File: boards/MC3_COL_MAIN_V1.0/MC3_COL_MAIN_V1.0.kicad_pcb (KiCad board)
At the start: 4 copper layers, 66 x 66 mm, 101 parts, among them J1 SUPPLY_IN, J10 MOTOR, J11 MOTOR, J12 CAN, J2 SWD, J3 ENC_leaf1, J4 ENC_leaf2, J5 ENC_leaf3, J6 ENC_leaf4, J7 MOTOR, J8 MOTOR, J9 MOTOR, Q1 AO4407C, SW1 SKRKAEE020, U1 AMS1117-3.3, U2 STM32F412RET6, U3 DRV8214RTER, U4 DRV8214RTER, U5 DRV8214RTER, U6 DRV8214RTER, U7 DRV8214RTER, U8 TJA1051T/3, Y1 8MHz

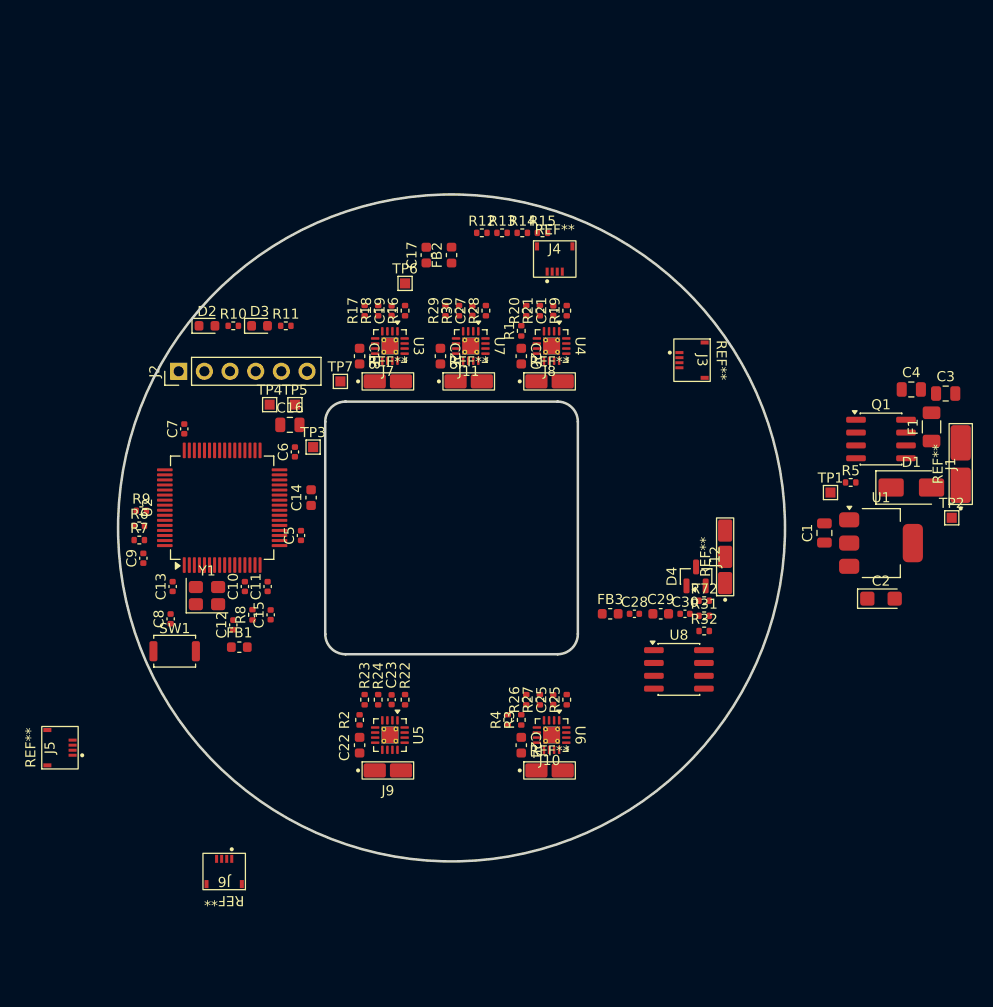
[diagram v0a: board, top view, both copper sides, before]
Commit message: PCB: user-facing items flipped to B.Cu; leaf3 pattern of record
Flipped 13 footprints to the back so they stay reachable once the board is
mounted component-face-toward-the-mechanism: J2 SWD, SW1 reset, D2/D3 LEDs,
J1 supply pads, J12 CAN pads, TP1-TP7. 88 footprints remain on F.Cu.

Of those, only SW1, D2 and D3 have any assembly cost - the pads are bare copper
and J2 is through-hole, so the SMT process stays single-sided unless those three
stay on the back. Noted so the choice can be reversed cheaply.

DRC after the flip: 275 unconnected (nothing routed yet), no new errors;
warnings 296 -> 229 as the user's hand-deleted REF** texts came out.

Board also carries the user's leaf3 rework: the whole block rotated one 90 deg
step and moved outboard, driver at r=25.2 and motor pads at r=26.6, pads facing
the rim. MIGRATION records the turned pattern as the block of record and marks
the placement of leaf1/leaf2/leaf4/yaw as the user's, per their decision.

flip_component has no IPC path - it writes the file directly and refuses while
KiCad is running, so further flips are a quit-KiCad operation.

Co-Authored-By: Claude Opus 5 (1M context) <noreply@anthropic.com>
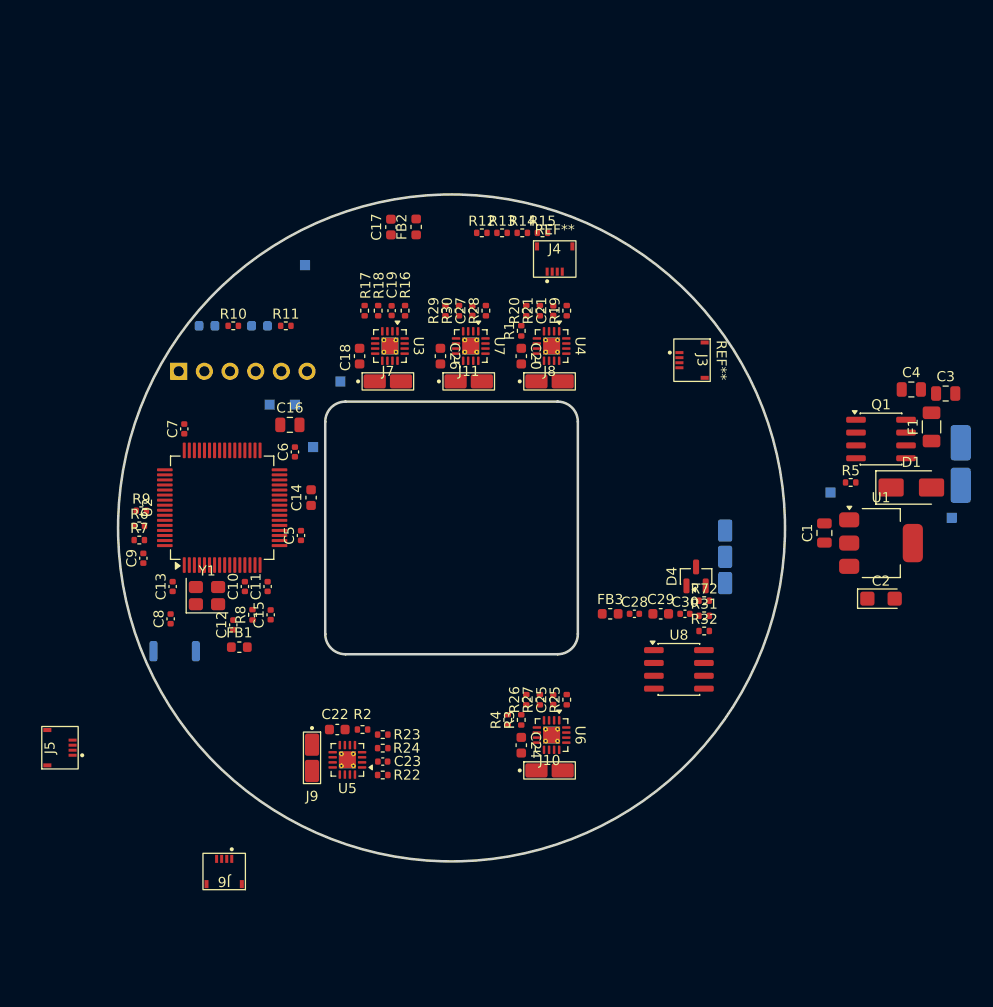
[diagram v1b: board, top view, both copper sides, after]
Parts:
- D2, D3, J1, J12, J2, SW1, TP1, TP2, TP3, TP4, TP5, TP6, TP7: moved to B.Cu
- moved TP6 10.1 mm to (85.5, 74.0)
- moved R22 7.77 mm to (93.2, 124.5), turned to 0 degrees
- moved J9 7.61 mm to (86.2, 122.8), turned to -90 degrees
- moved C23 6.18 mm to (93.2, 123.1), turned to 0 degrees
- moved U5 4.87 mm to (89.7, 123.0), turned to 180 degrees
- moved R24 4.81 mm to (93.2, 121.8), turned to 0 degrees
- moved FB2 4.47 mm to (96.5, 70.2)
- moved C17 4.47 mm to (94.0, 70.2)
- moved R23 3.89 mm to (93.2, 120.5), turned to 0 degrees
- moved C22 2.70 mm to (88.7, 120.0), turned to 180 degrees
- moved R2 0.99 mm to (91.2, 120.0), turned to 0 degrees
- turned J1 to -90 degrees
- turned J12 to -90 degrees
- turned J2 to -90 degrees

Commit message: PCB: add the three copper zones (In1 GND, In2 +3V3, B.Cu GND)
Written with KiCad quit - add_zone has no IPC path. Each zone is a rectangle
loosely enclosing the board (66,66)-(134,134); KiCad clips the fill to the
outline and to the central aperture, so no polygon has to trace the disc.
Clearance 0.2, min width 0.2, matching the MOTOR/VM netclass clearance.

Plane allocation changed from the earlier plan (In2 was to be VM). The pad
counts are lopsided - +3V3 has 55 pads spread across the whole disc while VM
has 20 clustered ones - so In2 carries +3V3 and VM becomes a 2.0 mm trunk on
F.Cu, where the high-current loop can be seen and shaped. The 2 A polyfuse
caps sustained VM current, so the trunk is thermally easy. A higher-priority
VM island can be dropped onto In2 under the motor annulus once the channels
are placed, which gets both.

In1 stays solid GND: it is the return reference 0.21 mm below every F.Cu
trace, which is what makes top-side routing good.

The zones carry no fill data yet - they need Edit > Fill All Zones (B) and a
save in KiCad before connectivity counts them. Expect unconnected to fall from
271 to roughly 120 at that point.

Co-Authored-By: Claude Opus 5 (1M context) <noreply@anthropic.com>
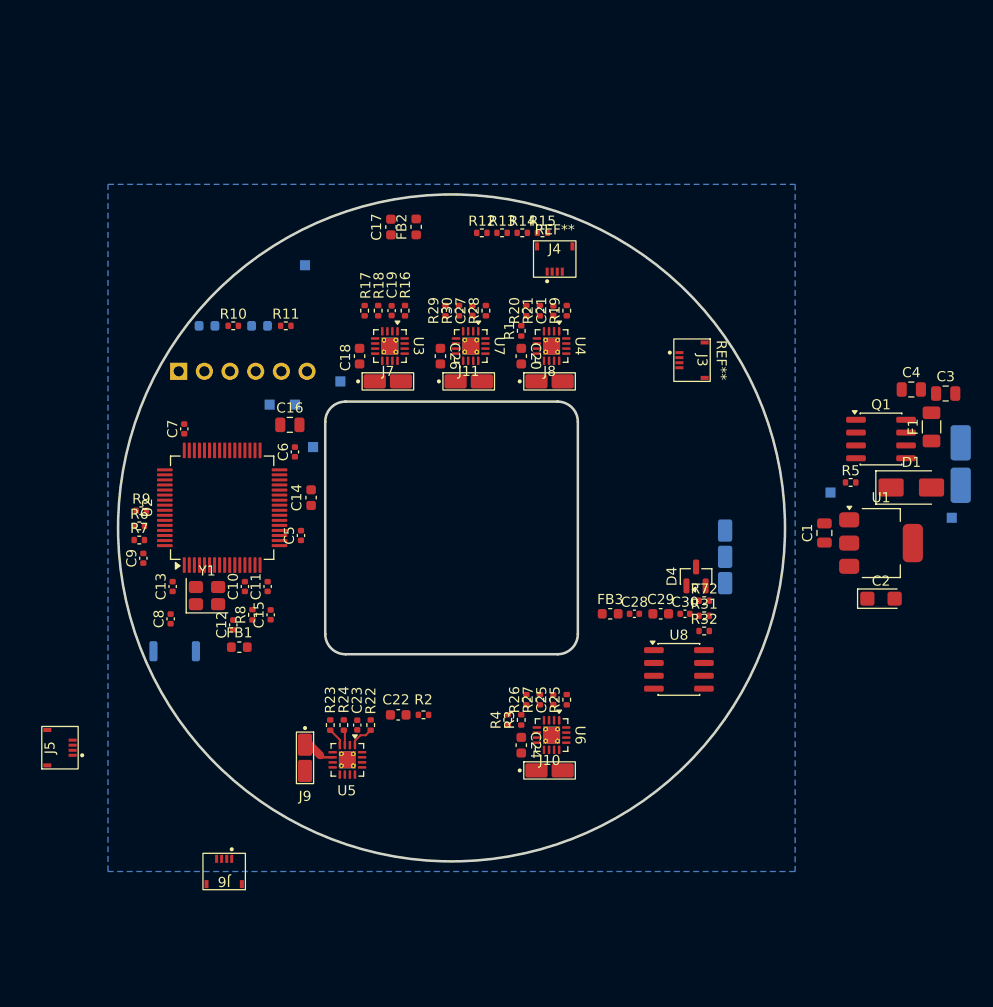
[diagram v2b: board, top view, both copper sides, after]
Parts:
- moved C22 6.21 mm to (94.7, 118.5)
- moved R2 6.21 mm to (97.2, 118.5)
- moved R23 5.28 mm to (88.0, 119.5), turned to -90 degrees
- moved R22 5.08 mm to (92.0, 119.5), turned to 90 degrees
- moved R24 4.48 mm to (89.3, 119.5), turned to -90 degrees
- moved C23 4.40 mm to (90.7, 119.5), turned to 90 degrees
- moved J9 0.69 mm to (85.5, 122.8)
- turned U5 to -90 degrees
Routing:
- net /leaf3/OUT1: track 0.00 -> 3.25 mm
- net IPROPI_leaf3: track 0.00 -> 2.42 mm
- net nFAULT_leaf3: track 0.00 -> 1.86 mm
- net RC_OUT_leaf3: track 0.00 -> 1.52 mm
- added copper zone on In2.Cu, net +3V3
- added copper zone on B.Cu, net GND
- added copper zone on In1.Cu, net GND

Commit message: PCB: F.Cu GND pour, 34 GND stitching vias, first leaf3 routing
User added the F.Cu GND zone and set In1 to solid pad connection; Konnect added
34 through-hole stitching vias (0.6/0.3) on a ~7 mm grid, positions computed
against all 415 pads and the existing traces so none creates a clearance error.
User also rotated U5 to -90 so the driver's power edge (pins 5-8) now faces the
motor pads, and routed the first leaf3 traces (21 segments).

Connectivity: 275 -> 204 unconnected. The whole gain came from the F.Cu pour;
the stitching vias moved nothing, because each DRV8214 exposed pad already
carries four through-holes that bridged F.Cu / In1 / B.Cu, so GND was already
one body. The vias are kept for return-path quality and to tie in pour islands
as routing fragments the top layer.

What is left, by net: +3V3 42 pads, VM 14, signals ~120, and GND just 7 - and
all 7 (C2.2, C4.2, D1.2, J1.2, R5.2, U1.1, J6.2) are parts still parked outside
the board outline, where no zone fills.

Co-Authored-By: Claude Opus 5 (1M context) <noreply@anthropic.com>
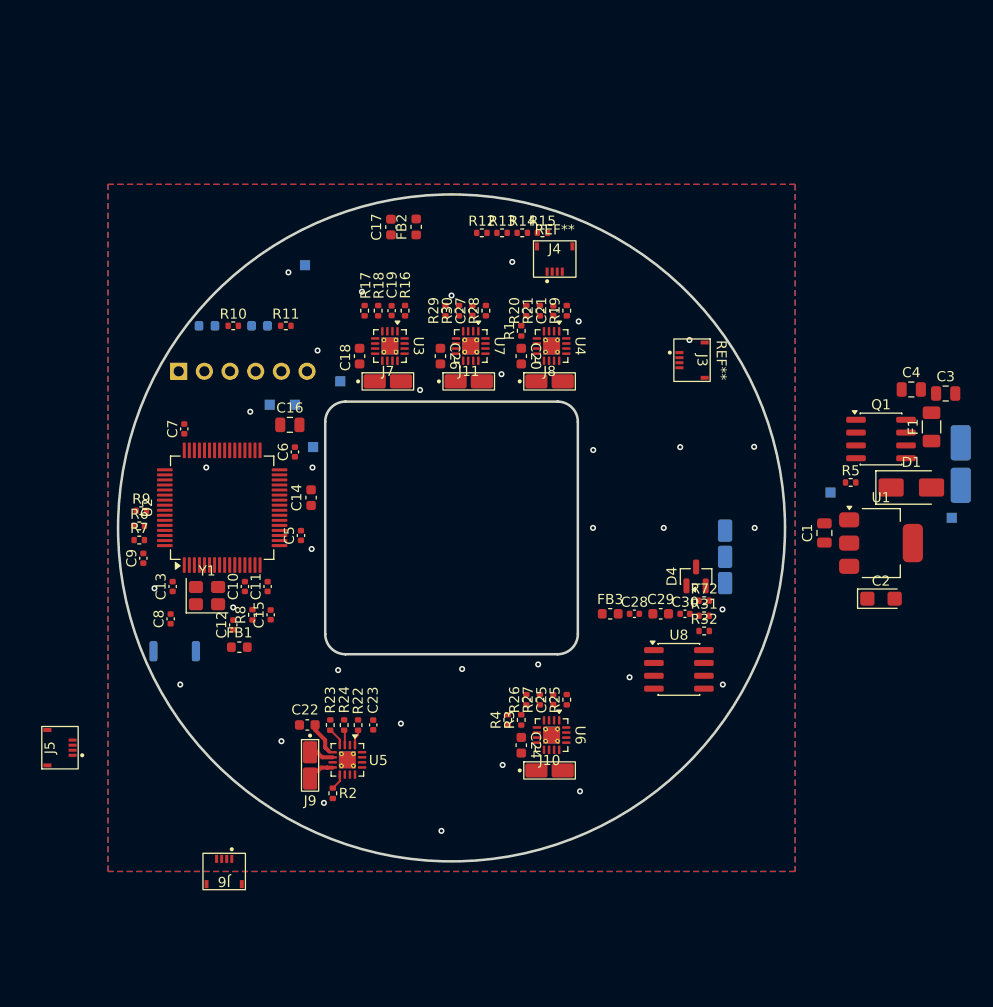
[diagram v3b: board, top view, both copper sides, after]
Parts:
- moved R2 11.9 mm to (88.2, 126.3), turned to 90 degrees
- moved C22 9.06 mm to (85.7, 119.5)
- moved C23 1.58 mm to (92.2, 119.5)
- moved R22 1.25 mm to (90.8, 119.5)
- moved J9 0.90 mm to (86.0, 123.5)
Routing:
- net VM: track 0.00 -> 3.17 mm
- net /leaf3/OUT2: track 0.00 -> 2.87 mm
- net /leaf3/A1: track 0.00 -> 1.63 mm
- net IPROPI_leaf3: track 2.42 -> 1.60 mm
- net GND: vias 0 -> 34
- added copper zone on F.Cu, net GND

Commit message: Schematic: local VM bulk per channel + LDO input filter
Two changes to isolate motor switching noise from the +3V3 rail.

1. MotorChannel.kicad_sch gains a 10 uF 0805 (C15850) from VM to GND beside
   the existing 1 uF. One symbol in the shared sheet, so five caps on the
   board. TI asks for 0.1 uF plus bulk at VM and the board bulk was over in
   the power block, at the far end of the VM trunk.

2. Power.kicad_sch gains FB4 + C32 on a new VM_LDO net between VM and the
   AMS1117's VI pin, plus a PWR_FLAG the new net needs for ERC. The regulator
   was a direct path from the motor rail to +3V3 - its PSRR is down to about
   30 dB by 100 kHz, well inside the PWM band.

FB4 is C14709 (Murata BLM18PG121SN1D, 120R@100MHz, 2 A, 50 mohm), NOT the 600R
C1002 used on VDDA and VCAN5 - that part is 200 mA / 450 mohm and would have
been marginal on current and cost ~110 mV of the AMS1117's dropout headroom.

Flagged in MIGRATION: FB4 with C32 forms an LC at roughly 115 kHz with Q ~2.8,
which could amplify rather than attenuate if the motor PWM lands near it. Needs
the firmware's PWM frequency to close, and damping (tantalum or an R leg) if it
does - shrinking C32 would make it worse, not better.

ERC: 0 errors, the same 8 intentional same_local_global warnings as before.

Co-Authored-By: Claude Opus 5 (1M context) <noreply@anthropic.com>
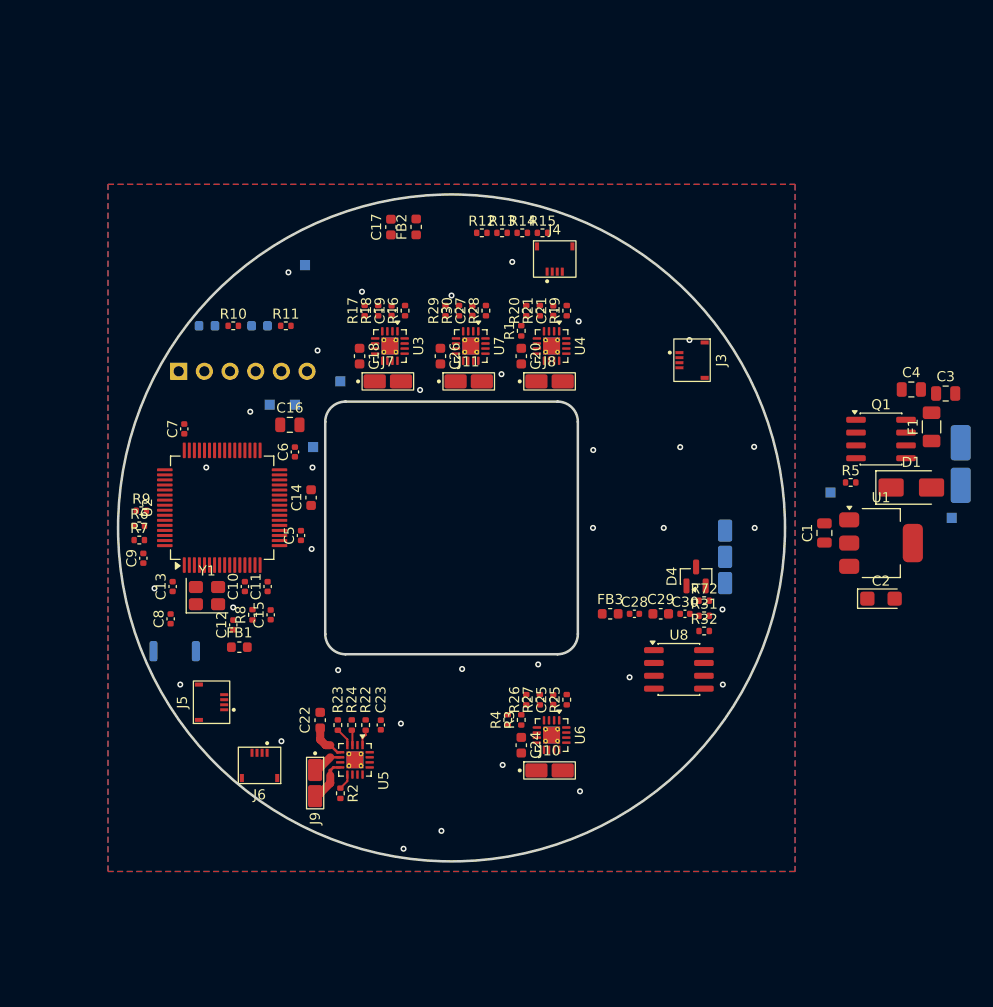
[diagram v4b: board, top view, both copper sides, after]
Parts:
- moved J5 15.7 mm to (76.2, 117.2)
- moved J6 11.1 mm to (81.0, 123.5)
- moved J9 1.82 mm to (86.5, 125.2)
- moved C22 1.36 mm to (87.0, 119.0), turned to 90 degrees
- moved C23 0.75 mm to (93.0, 119.5)
- moved R2 0.75 mm to (89.0, 126.3)
- moved R22 0.75 mm to (91.5, 119.5)
- moved R23 0.75 mm to (88.8, 119.5)
- moved R24 0.75 mm to (90.1, 119.5)
- moved U5 0.75 mm to (90.4, 123.0)
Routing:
- net /leaf3/OUT2: track 2.87 -> 4.52 mm

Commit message: Schematic: new channel cap goes in as C? so annotation can assign per-instance refs
Adding it as C31 put that string in the symbol-level Reference property, so all
five sheet instances fell back to it and eeschema reported four duplicates.
Keep-existing annotation will not touch them because they do not look
unannotated. Reference is now C? on the property and on all five instance
paths; value, footprint, LCSC, MPN and the Note field are unchanged.

Co-Authored-By: Claude Opus 5 (1M context) <noreply@anthropic.com>
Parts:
- moved SW1 3.70 mm to (75.8, 110.2)

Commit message: PCB: 8 new footprints from the schematic, fab attributes restored
Update PCB from Schematic applied: C31/C33/C34/C35/C36 (the per-channel VM
bulk, one per instance), C32 and FB4 (LDO input filter), plus JP1 - the solder
jumper the schematic still carries while the board uses R72. Net /Power/VM_LDO
created and U1 pin 3 reconnected to it. 101 -> 109 footprints.

That update strips fabrication attributes, because it syncs them from the
schematic symbol rather than the footprint library: J1 and J7-J11 dropped
exclude_from_pos_files/exclude_from_bom, and TP1-TP7 lost their attr line
entirely. Repaired with Update Footprints from Library scoped to all footprints
with only "reset fabrication attributes" ticked - the first attempt silently
covered just the 8 newly added parts because they were still selected.

Verified after: all 109 carry an attr line, J1/J7-J11 and TP1-TP7 are excluded
from BOM and position files again, and leaf3's hand-arranged silkscreen offsets
are untouched (the text reset box was deliberately left clear).

Still open: J12's library footprint (SolderPads_3x) never had the exclusions, so
the CAN pads remain in the BOM/PnP; JP1 needs resolving against R72; and the 8
new footprints are parked off-board awaiting placement.

Co-Authored-By: Claude Opus 5 (1M context) <noreply@anthropic.com>
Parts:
- added C31: 10uF, MC3_COL_MAIN:C_0805_2012Metric, F.Cu at (142.7, 130.0)
- added C32: 10uF, MC3_COL_MAIN:C_0805_2012Metric, F.Cu at (136.2, 120.0)
- added C33: 10uF, MC3_COL_MAIN:C_0805_2012Metric, F.Cu at (142.7, 120.0)
- added C34: 10uF, MC3_COL_MAIN:C_0805_2012Metric, F.Cu at (149.1, 125.0)
- added C35: 10uF, MC3_COL_MAIN:C_0805_2012Metric, F.Cu at (142.7, 125.0)
- added C36: 10uF, MC3_COL_MAIN:C_0805_2012Metric, F.Cu at (149.1, 120.0)
- added FB4: 120R@100MHz 2A, MC3_COL_MAIN:L_0603_1608Metric, F.Cu at (136.0, 122.8)
- added JP1: TERM, MC3_COL_MAIN:SolderJumper-2_P1.3mm_Bridged_RoundedPad1.0x1.5mm, F.Cu at (136.2, 127.8)
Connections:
- U1 pad 3: VM -> /Power/VM_LDO
